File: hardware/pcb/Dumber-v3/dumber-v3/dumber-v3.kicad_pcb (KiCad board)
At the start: 2 copper layers, 88 x 86 mm, 46 parts, among them P1 USB_C_Plug_GCT_USB4125, Q1 PMN52XP, SW1 SW_Push, U1 XBee_SMT, U2 STM32L031C6Tx, U3 LTC2954, U4 L6924U, U5 NCV5171, U6 DIO6010

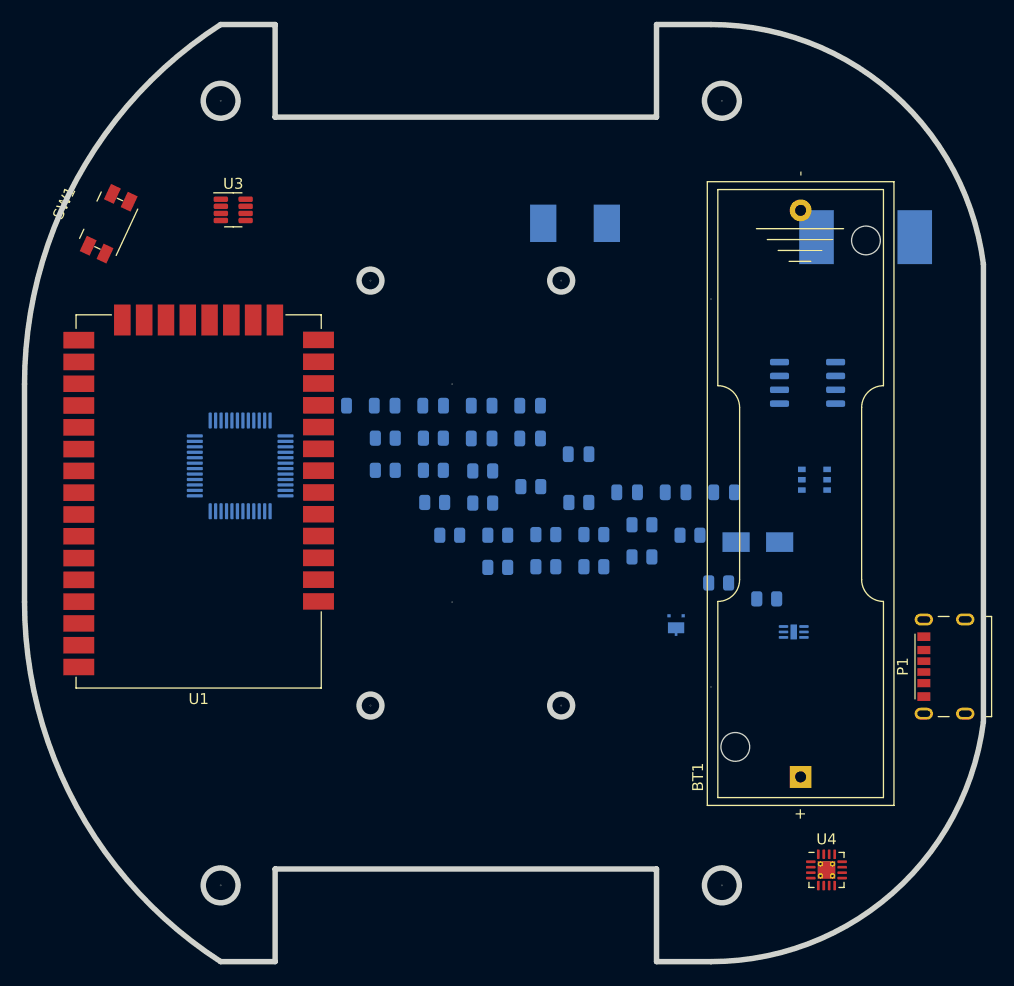
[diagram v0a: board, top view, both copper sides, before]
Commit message: Schema complet, projet logiciel demarré
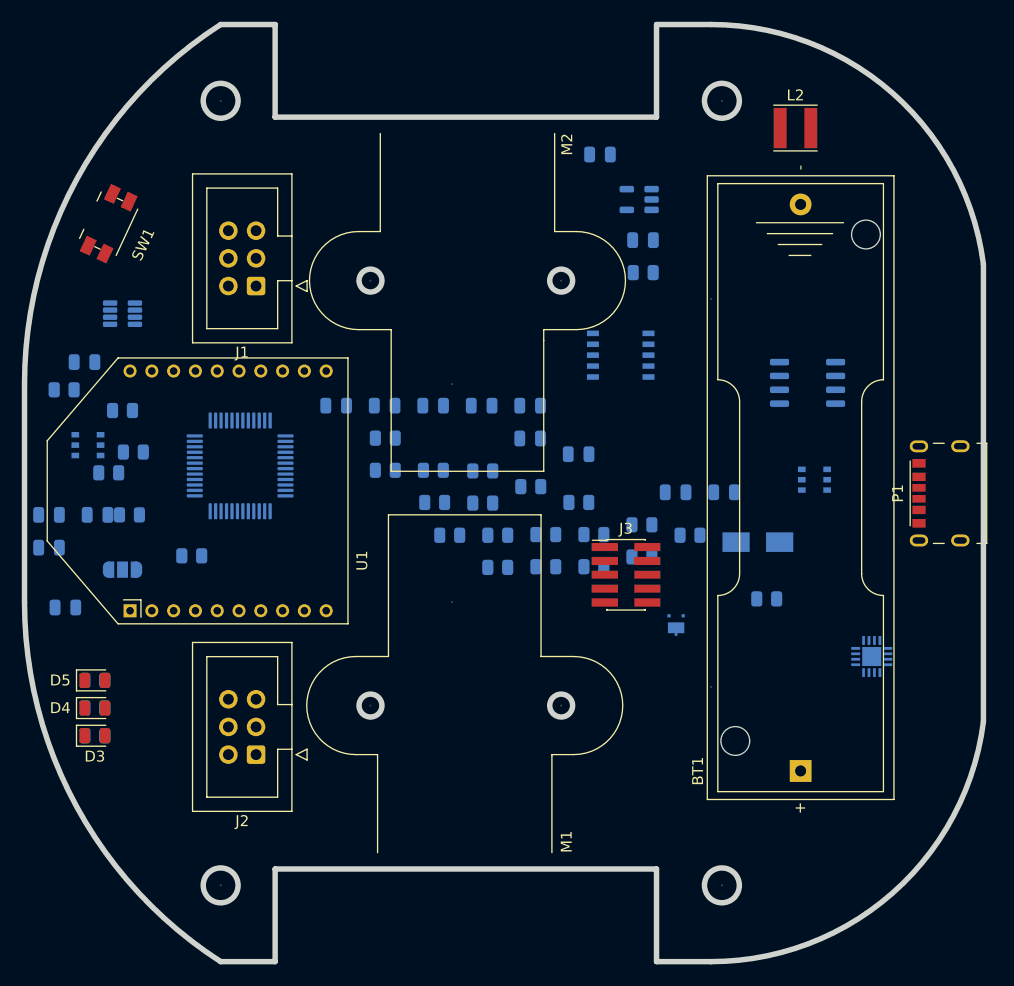
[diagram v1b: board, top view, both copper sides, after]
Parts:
- removed L1: 3.3µH, Inductor_SMD:L_Vishay_IHLP-2525
- added C12: C, Capacitor_SMD:C_0805_2012Metric, B.Cu at (113.5, 116.5)
- added C13: C, Capacitor_SMD:C_0805_2012Metric, B.Cu at (116.5, 108.0)
- added C14: C, Capacitor_SMD:C_0805_2012Metric, B.Cu at (112.0, 108.0)
- added C15: C, Capacitor_SMD:C_0805_2012Metric, B.Cu at (112.0, 111.0)
- added C16: 100nF, Capacitor_SMD:C_0805_2012Metric, B.Cu at (115.3, 94.0)
- added D3: LED, Diode_SMD:D_0805_2012Metric, F.Cu at (116.2, 128.3)
- added D4: LED, Diode_SMD:D_0805_2012Metric, F.Cu at (116.2, 125.7)
- added D5: LED, Diode_SMD:D_0805_2012Metric, F.Cu at (116.2, 123.2)
- added J1: Conn_02x03_Odd_Even, Connector_IDC:IDC-Header_2x03_P2.54mm_Vertical, F.Cu at (131.0, 87.0)
- added J2: Conn_02x03_Odd_Even, Connector_IDC:IDC-Header_2x03_P2.54mm_Vertical, F.Cu at (131.0, 130.0)
- added J3: Conn_02x05_Odd_Even, Connector_PinHeader_1.27mm:PinHeader_2x05_P1.27mm_Vertical_SMD, F.Cu at (164.9, 113.5)
- added JP1: Jumper_3_Bridged12, Jumper:SolderJumper-3_P1.3mm_Open_RoundedPad1.0x1.5mm_NumberLabels, B.Cu at (118.7, 113.0)
- added M1: Motor, INSA:Motor Pololu HPCB with encoder, F.Cu at (150.2, 150.0)
- added M2: Motor, INSA:Motor Pololu HPCB with encoder, F.Cu at (150.4, 62.0)
- added Q2: PMN52XP, Package_SO:TSOP-6_1.65x3.05mm_P0.95mm, B.Cu at (115.6, 101.6)
- added R22: R, Resistor_SMD:R_0805_2012Metric, B.Cu at (116.2, 125.7)
- added R23: R, Resistor_SMD:R_0805_2012Metric, B.Cu at (116.2, 123.2)
- added R24: 100K, Resistor_SMD:R_0805_2012Metric, B.Cu at (117.5, 104.1)
- added R25: 10R, Resistor_SMD:R_0805_2012Metric, B.Cu at (118.7, 98.4)
- added R26: 10K, Resistor_SMD:R_0805_2012Metric, B.Cu at (113.4, 96.5)
- added R27: 100K, Resistor_SMD:R_0805_2012Metric, B.Cu at (119.4, 108.0)
- added R28: 100K, Resistor_SMD:R_0805_2012Metric, B.Cu at (125.1, 111.8)
- added R29: 100K, Resistor_SMD:R_0805_2012Metric, B.Cu at (119.7, 102.2)
- added U7: A3909, Package_SO:SSOP-10_3.9x4.9mm_P1.00mm, B.Cu at (164.5, 93.3)
- C11, C6: value 10µF -> 1µF
- C5: value 10nF -> 100nF
- C9: value 22pF -> 100pF
- L2: footprint Inductor_SMD:L_Vishay_IHLP-4040 -> Inductor_SMD:L_Taiyo-Yuden_MD-4040; moved to F.Cu
- R15: value 33.2K -> 1M
- R16: value 10K -> R
- R17, R19: value R -> 150K
- R18, R20: value R -> 100K
- U1: value XBee_SMT -> XBEE-3; footprint RF_Module:Digi_XBee_SMT -> INSA:XBEE-3-TH
- U2: value STM32L031C6Tx -> STM32L010C6Tx
- U3: moved to B.Cu
- U4: footprint Package_DFN_QFN:VQFN-16-1EP_3x3mm_P0.5mm_EP1.6x1.6mm_ThermalVias -> INSA:L6924UTR; moved to B.Cu
- U6: value DIO6010 -> TC1186; footprint Package_DFN_QFN:DFN-6-1EP_2x2mm_P0.5mm_EP0.6x1.37mm -> Package_TO_SOT_SMD:SOT-23-5
- moved R16 58.9 mm to (116.2, 128.3), turned to 0 degrees
- moved U6 42.1 mm to (166.2, 79.1)
- moved C11 31.1 mm to (162.6, 74.9)
- moved R15 24.5 mm to (166.5, 85.8)
- moved C9 23.5 mm to (166.5, 82.8)
- moved U4 20.0 mm to (187.5, 121.0), turned to 180 degrees
- moved U1 18.2 mm to (139.4, 118.0), turned to 90 degrees
- moved P1 15.9 mm to (191.2, 110.5)
- moved U3 13.9 mm to (118.7, 89.5), turned to 180 degrees
- moved L2 11.9 mm to (180.5, 72.5), turned to 0 degrees
- moved BT1 0.54 mm to (181.0, 131.5)
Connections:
- C9 pad 1: +2V5 -> Net-(C9-Pad1)
- C9 pad 2: Net-(C9-Pad2) -> GND
- R15 pad 1: Net-(C9-Pad2) -> Net-(C9-Pad1)
- R15 pad 2: +2V5 -> Net-(C6-Pad1)
- R16 pad 1: GND -> /Cpu/LED_ROUGE
- R16 pad 2: Net-(C9-Pad2) -> Net-(D3-Pad2)
- R17 pad 2: /Power_Charge/USB_SENSE -> /Cpu/USB_SENSE
- R18 pad 1: /Power_Charge/USB_SENSE -> /Cpu/USB_SENSE
- R19 pad 2: /Power_Charge/BATTERY_SENSE -> /Cpu/BATTERY_SENSE
- R20 pad 1: /Power_Charge/BATTERY_SENSE -> /Cpu/BATTERY_SENSE
- R3 pad 2: /Power_Charge/CHARGER_ST1 -> /Cpu/CHARGER_ST1
- R4 pad 2: /Power_Charge/SHUTDOWN -> /Cpu/SHUTDOWN
- R5 pad 2: /Power_Charge/CHARGER_ST2 -> /Cpu/CHARGER_ST2
- R6 pad 2: /Power_Charge/BUTTON_SENSE -> /Cpu/BUTTON_SENSE
- U1 pad 1: unconnected-(U1-Pad1) -> +2V5
- U1 pad 10: unconnected-(U1-Pad10) -> GND
- U1 pad 14: unconnected-(U1-Pad14) -> (no net)
- U1 pad 2: unconnected-(U1-Pad2) -> /Cpu/USART_RX
- U1 pad 3: unconnected-(U1-Pad3) -> /Cpu/USART_TX
- U1 pad 5: unconnected-(U1-Pad5) -> /Cpu/XBEE_RESET
- U1 pad 8: unconnected-(U1-Pad8) -> (no net)
- U2 pad 1: unconnected-(U2-Pad1) -> /Cpu/ENCGAUCHE_A
- U2 pad 10: unconnected-(U2-Pad10) -> /Cpu/BATTERY_SENSE
- U2 pad 11: unconnected-(U2-Pad11) -> /Cpu/PWM_GAUCHE_B
- U2 pad 12: unconnected-(U2-Pad12) -> /Cpu/ENCDROIT_A
- U2 pad 13: unconnected-(U2-Pad13) -> /Cpu/ENCDROIT_B
- U2 pad 15: unconnected-(U2-Pad15) -> /Cpu/ENCGAUCHE_B
- U2 pad 18: unconnected-(U2-Pad18) -> /Cpu/PWM_DROIT_A
- U2 pad 19: unconnected-(U2-Pad19) -> /Cpu/PWM_DROIT_B
- U2 pad 21: unconnected-(U2-Pad21) -> /Cpu/USART_TX
- U2 pad 22: unconnected-(U2-Pad22) -> /Cpu/USART_RX
- U2 pad 23: unconnected-(U2-Pad23) -> GND
- U2 pad 24: unconnected-(U2-Pad24) -> +2V5
- U2 pad 25: unconnected-(U2-Pad25) -> /Cpu/LED_ROUGE
- U2 pad 26: unconnected-(U2-Pad26) -> /Cpu/LED_ORANGE
- U2 pad 27: unconnected-(U2-Pad27) -> /Cpu/LED_VERTE
- U2 pad 28: unconnected-(U2-Pad28) -> /Cpu/SHUTDOWN_ENC
- U2 pad 29: unconnected-(U2-Pad29) -> /Cpu/PWM_GAUCHE_A
- U2 pad 34: unconnected-(U2-Pad34) -> /Cpu/SWDIO
- U2 pad 35: unconnected-(U2-Pad35) -> GND
- U2 pad 36: unconnected-(U2-Pad36) -> +2V5
- U2 pad 37: unconnected-(U2-Pad37) -> /Cpu/SWCLK
- U2 pad 38: unconnected-(U2-Pad38) -> /Cpu/XBEE_RESET
- U2 pad 39: unconnected-(U2-Pad39) -> /Cpu/BUTTON_SENSE
- U2 pad 40: unconnected-(U2-Pad40) -> /Cpu/USB_SENSE
- U2 pad 42: unconnected-(U2-Pad42) -> /Cpu/CHARGER_ST2
- U2 pad 43: unconnected-(U2-Pad43) -> /Cpu/CHARGER_ST1
- U2 pad 44: unconnected-(U2-Pad44) -> Net-(U2-Pad44)
- U2 pad 45: unconnected-(U2-Pad45) -> /Cpu/SHUTDOWN_5V
- U2 pad 46: unconnected-(U2-Pad46) -> /Cpu/SHUTDOWN
- U2 pad 47: unconnected-(U2-Pad47) -> GND
- U2 pad 48: unconnected-(U2-Pad48) -> +2V5
- U2 pad 7: unconnected-(U2-Pad7) -> /Cpu/RESET
- U2 pad 8: unconnected-(U2-Pad8) -> GND
- U2 pad 9: unconnected-(U2-Pad9) -> +2V5
- U3 pad 5: /Power_Charge/SHUTDOWN -> /Cpu/SHUTDOWN
- U3 pad 8: /Power_Charge/BUTTON_SENSE -> /Cpu/BUTTON_SENSE
- U4 pad 3: /Power_Charge/CHARGER_ST2 -> /Cpu/CHARGER_ST2
- U4 pad 4: /Power_Charge/CHARGER_ST1 -> /Cpu/CHARGER_ST1
- U5 pad 4: /Power_Charge/SHUTDOWN_5V -> /Cpu/SHUTDOWN_5V
- U6 pad 1: unconnected-(U6-Pad1) -> Net-(C6-Pad1)
- U6 pad 2: Net-(C6-Pad1) -> GND
- U6 pad 4: Net-(L1-Pad1) -> Net-(C9-Pad1)
- U6 pad 5: GND -> +2V5

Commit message: PCB fini
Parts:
- added C17: 100nF, Capacitor_SMD:C_0805_2012Metric, B.Cu at (156.2, 106.0)
- added C18: 100nF, Capacitor_SMD:C_0805_2012Metric, B.Cu at (159.4, 114.6)
- added C19: 100nF, Capacitor_SMD:C_0805_2012Metric, B.Cu at (144.8, 119.7)
- added C20: 100nF, Capacitor_SMD:C_0805_2012Metric, B.Cu at (141.6, 111.8)
- D2: moved to F.Cu
- moved C7 53.1 mm to (184.8, 130.5), turned to 90 degrees
- moved C2 51.1 mm to (118.4, 107.3)
- moved Q1 50.9 mm to (131.4, 101.0)
- moved C3 50.9 mm to (188.6, 106.0), turned to -90 degrees
- moved R27 48.1 mm to (167.0, 114.7), turned to 90 degrees
- moved C16 47.1 mm to (152.7, 122.6)
- moved R4 44.8 mm to (122.6, 99.7)
- moved R26 44.4 mm to (149.9, 121.9), turned to 90 degrees
- moved R29 44.0 mm to (161.9, 114.7), turned to 90 degrees
- moved C12 42.7 mm to (150.4, 95.0)
- moved C4 41.5 mm to (184.8, 115.6), turned to 90 degrees
- moved C1 41.4 mm to (114.9, 101.6), turned to -90 degrees
- moved R28 39.5 mm to (164.5, 114.7), turned to -90 degrees
- moved R8 39.1 mm to (182.2, 89.7), turned to 90 degrees
- moved D1 37.9 mm to (136.8, 100.0), turned to -90 degrees
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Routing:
- net GND: track 0.00 -> 434.1 mm, vias 0 -> 7
- net +2V5: track 0.00 -> 169.2 mm, vias 0 -> 8
- net +BATT: track 0.00 -> 135.7 mm, vias 0 -> 3
- net /Cpu/SHUTDOWN_5V: track 0.00 -> 121.2 mm, vias 0 -> 4
- net VBUS: track 0.00 -> 120.3 mm, vias 0 -> 8
- net /Cpu/SHUTDOWN: track 0.00 -> 90.5 mm, vias 0 -> 4
- net /Cpu/ENCGAUCHE_A: track 0.00 -> 85.9 mm, vias 0 -> 6
- net /Cpu/OUTDROIT_A: track 0.00 -> 84.9 mm, vias 0 -> 2
- net /Cpu/BUTTON_SENSE: track 0.00 -> 78.2 mm, vias 0 -> 4
- net /Cpu/RESET: track 0.00 -> 75.8 mm, vias 0 -> 5
- net /Cpu/OUTDROIT_B: track 0.00 -> 75.4 mm, vias 0 -> 2
- net Net-(C6-Pad1): track 0.00 -> 74.3 mm, vias 0 -> 4
- net Net-(J1-Pad3): track 0.00 -> 62.9 mm, vias 0 -> 5
- net +5V: track 0.00 -> 61.9 mm, vias 0 -> 2
- net /Cpu/ENCGAUCHE_B: track 0.00 -> 59.8 mm
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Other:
- board text added: "Dumber 3 V1 INSA-GEI 06/22"

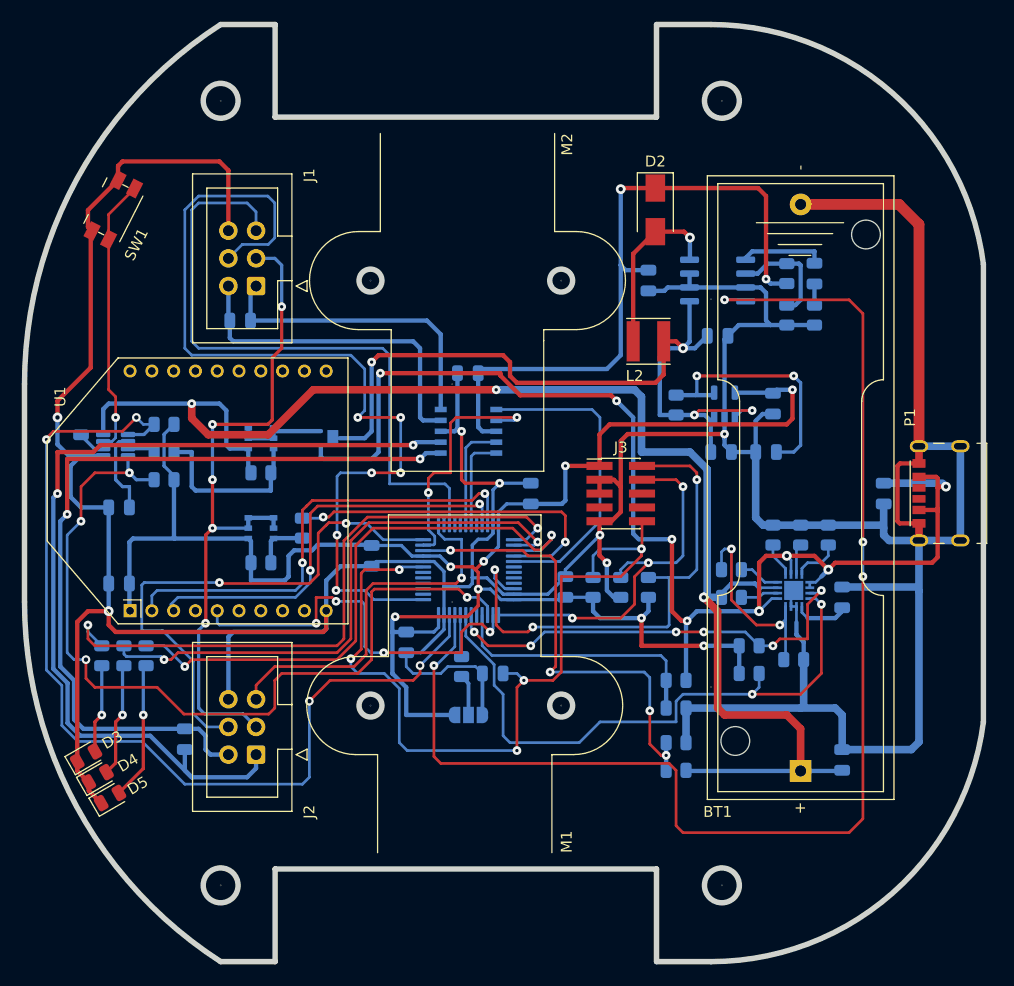
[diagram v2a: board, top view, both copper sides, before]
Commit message: nouvelle version pcb dumber + nouvelle version monietur en QT
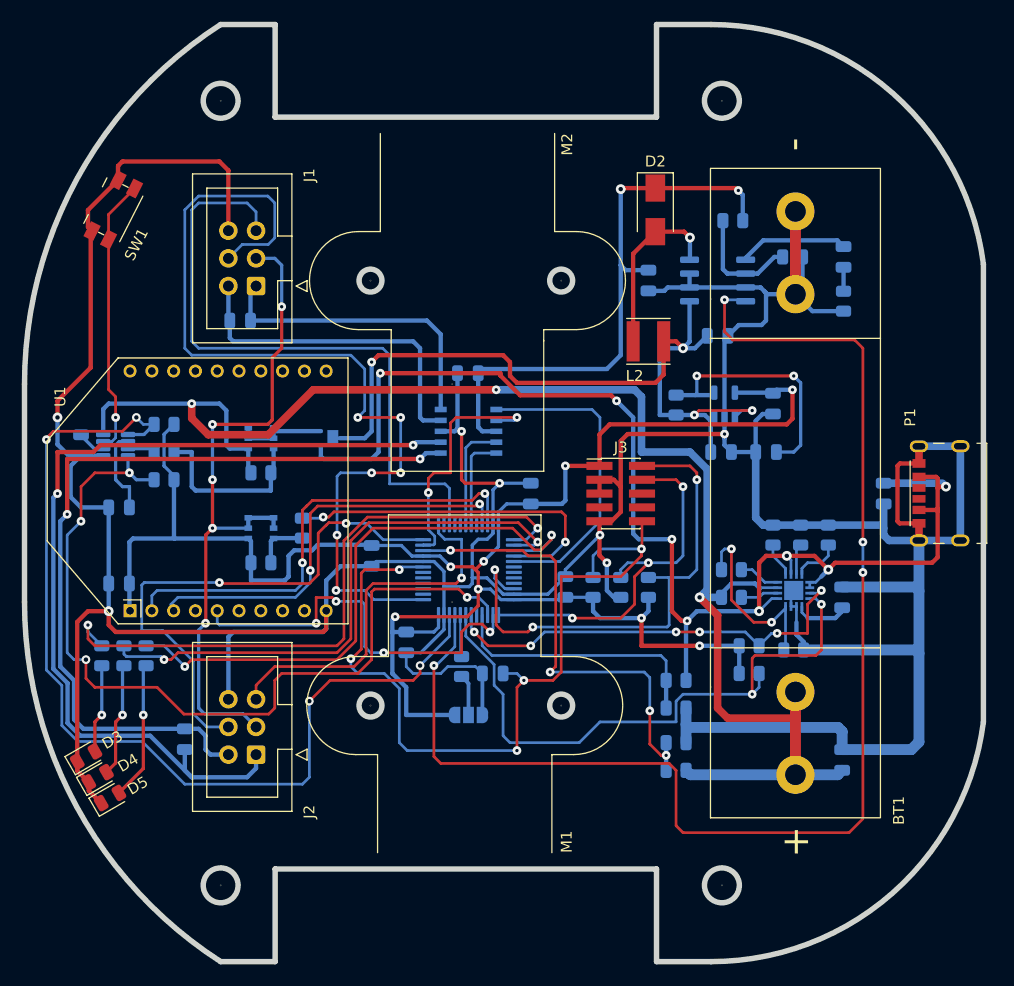
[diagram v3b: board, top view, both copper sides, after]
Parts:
- BT1: footprint Battery:BatteryHolder_Keystone_2460_1xAA -> INSA:Battery-14500
- C12, C13: value C -> 1µF
- C14, C15: value C -> 470nF
- R16, R22, R23: value R -> 1.5K
- moved BT1 25.5 mm to (180.5, 106.0)
- moved R10 6.94 mm to (174.8, 81.0), turned to 0 degrees
- moved R11 5.37 mm to (180.2, 84.3), turned to 180 degrees
- moved C5 3.07 mm to (184.9, 84.3)
- moved R8 2.96 mm to (184.9, 88.4)
- moved R9 0.89 mm to (180.3, 120.4)
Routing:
- net GND: track 434.1 -> 420.3 mm
- net +5V: track 61.9 -> 52.4 mm
- net +BATT: track 135.7 -> 139.7 mm
- net Net-(C5-Pad1): track 7.82 -> 10.1 mm
- net Net-(R7-Pad2): track 19.6 -> 17.9 mm
- net /Cpu/CHARGER_ST1: track 55.5 -> 56.2 mm
- net Net-(R10-Pad1): track 10.1 -> 10.7 mm
